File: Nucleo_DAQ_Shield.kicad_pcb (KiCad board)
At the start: 2 copper layers, 31 parts, among them J1 CONN_01X06, J2 CONN_01X06, J3 CONN_01X02, J4 CONN_01X02, J5 CONN_01X02, J6 CONN_COAXIAL, U1 4050, U10 ST_Nucleo144_F746ZG_CN10, U2 TL072, U3 LM7805CT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

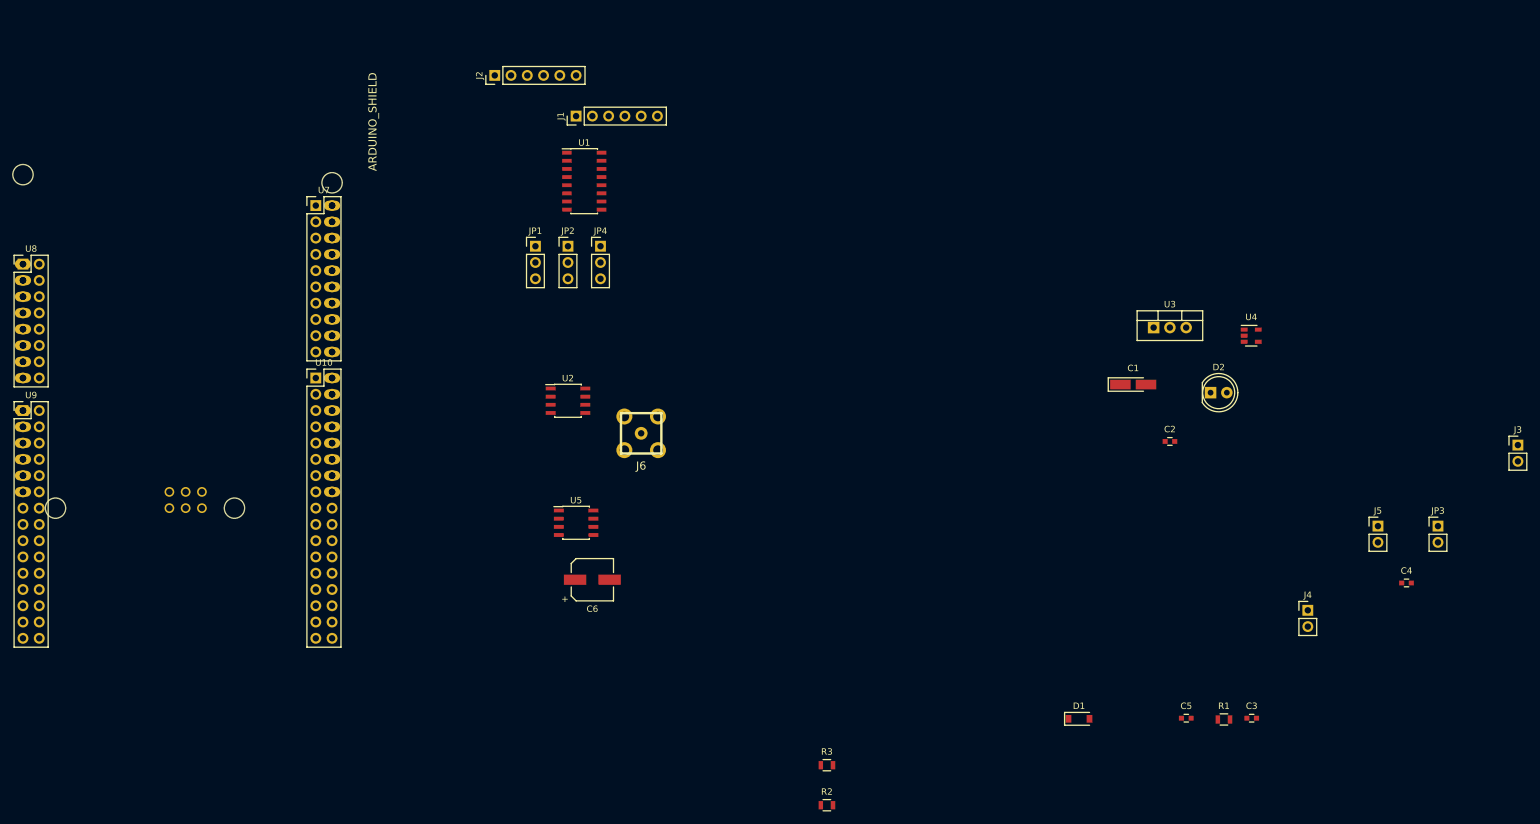
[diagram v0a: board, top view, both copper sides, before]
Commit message: Rough placement of all components
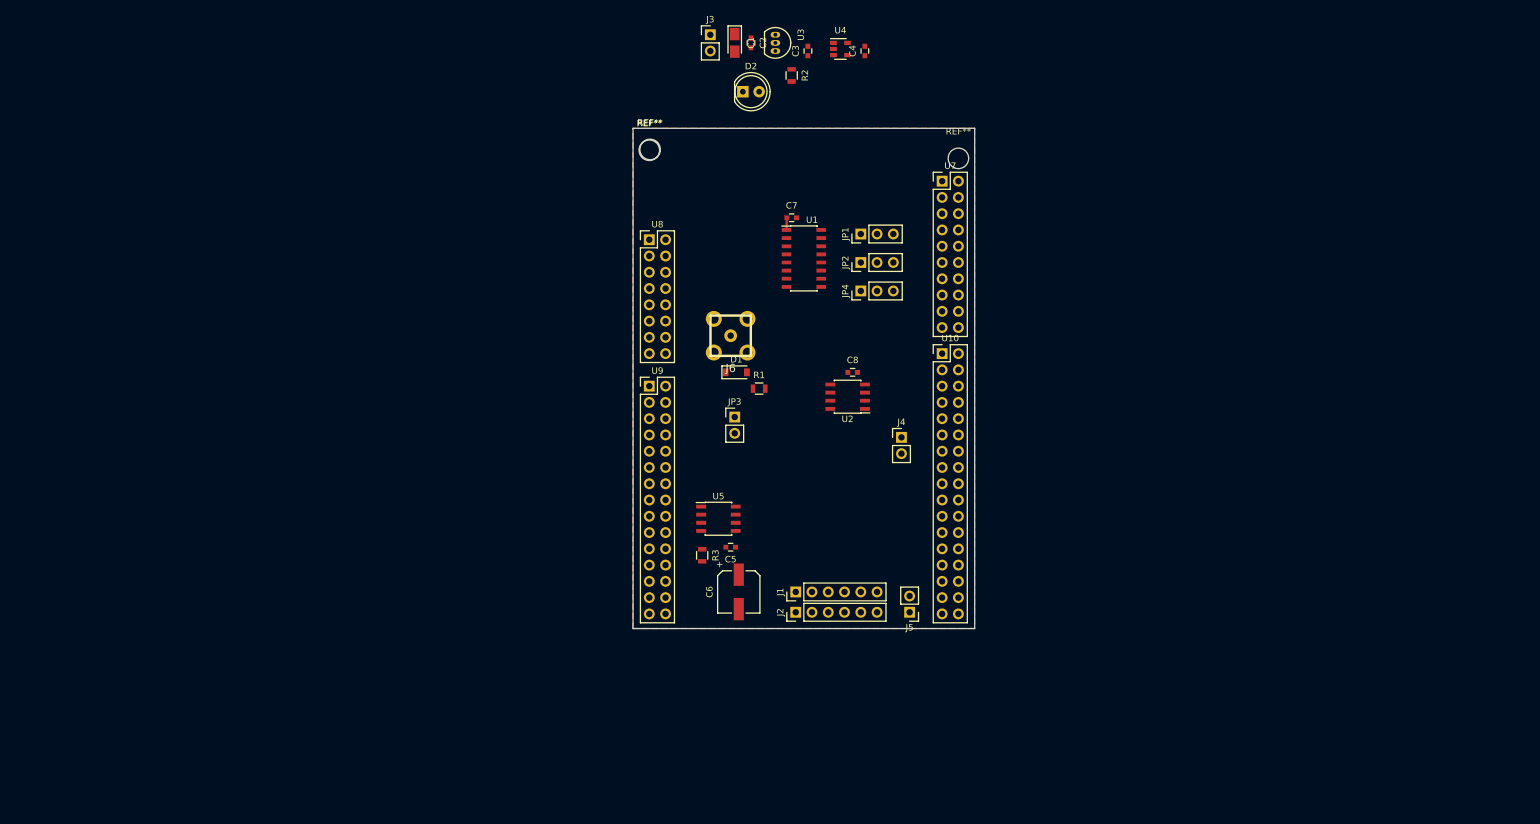
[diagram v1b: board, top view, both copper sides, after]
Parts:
- removed ARDUINO_SHIELD: val**, custom:ARDUINO_SHIELD
- added C7: 100nF, Capacitors_SMD:C_0603, F.Cu at (165.7, 62.9)
- added C8: 100nF, Capacitors_SMD:C_0603, F.Cu at (175.3, 87.0)
- added REF**: MountingHole_3.2mm_M3, Mounting_Holes:MountingHole_3.2mm_M3, F.Cu at (143.6, 52.2)
- added REF**: MountingHole_3.2mm_M3, Mounting_Holes:MountingHole_3.2mm_M3, F.Cu at (143.5, 52.3)
- added REF**: MountingHole_3.2mm_M3, Mounting_Holes:MountingHole_3.2mm_M3, F.Cu at (191.8, 53.6)
- C1: footprint Capacitors_Tantalum_SMD:CP_Tantalum_Case-A_EIA-3216-18_Hand -> Capacitors_Tantalum_SMD:CP_Tantalum_Case-A_EIA-3216-18_Reflow
- U3: footprint TO_SOT_Packages_THT:TO-220_Vertical -> TO_SOT_Packages_THT:TO-92_Inline_Narrow_Oval
- moved J3 141.4 mm to (153.0, 34.3)
- moved C3 125.1 mm to (168.3, 36.8), turned to 90 degrees
- moved C4 118.5 mm to (177.2, 36.8), turned to 90 degrees
- moved R2 114.1 mm to (165.7, 40.6), turned to 270 degrees
- moved JP3 111.1 mm to (156.8, 94.0)
- moved U10 97.9 mm to (189.2, 84.1)
- moved U7 97.9 mm to (189.2, 57.1)
- moved U8 97.9 mm to (143.5, 66.3)
- moved U9 97.9 mm to (143.5, 89.2)
- moved J2 96.1 mm to (166.4, 124.5)
- moved C2 90.3 mm to (159.4, 35.6), turned to 270 degrees
- moved R1 89.1 mm to (160.7, 89.5)
- moved D2 86.8 mm to (158.1, 43.2)
- moved C1 82.0 mm to (156.8, 35.6), turned to 270 degrees
- moved J1 81.8 mm to (166.4, 121.3)
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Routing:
- net +3.3VA: track 0.00 -> 2.40 mm
- added copper zone on F.Cu, net GND
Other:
- board outline added: 53.3 x 78.1 mm
- net class Default: clearance 0.2 -> 0.381; trace_width 0.25 -> 0.381
- rule trace_clearance: 0.2 -> 0.381

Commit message: --amend
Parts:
- added J7: CONN_01X02, Pin_Headers:Pin_Header_Straight_1x02_Pitch2.54mm, F.Cu at (174.0, 105.4)
- moved C7 43.0 mm to (177.8, 104.1)
- moved U1 43.0 mm to (179.7, 110.5)
- moved JP1 42.8 mm to (165.1, 106.7)
- moved JP2 41.0 mm to (165.1, 109.2)
- moved JP4 39.2 mm to (165.1, 111.8)
- moved C1 17.8 mm to (158.1, 53.3)
- moved C2 17.8 mm to (160.7, 53.3)
- moved C3 17.8 mm to (169.5, 54.6)
- moved C4 17.8 mm to (178.4, 54.6)
- moved D2 17.8 mm to (159.4, 61.0)
- moved J3 17.8 mm to (154.3, 52.1), turned to 270 degrees
- moved R2 17.8 mm to (167.0, 58.4)
- moved U3 17.8 mm to (164.5, 52.1)
- moved U4 17.8 mm to (174.6, 54.3)
- moved J4 14.9 mm to (177.8, 83.2)
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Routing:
- net +3.3VA: track 2.40 -> 0.00 mm

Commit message: Some progress on routing
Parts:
- moved R3 1.42 mm to (150.5, 114.9)
- moved JP1 1.27 mm to (165.1, 105.4)
- moved JP4 1.27 mm to (165.1, 113.0)
- moved C4 0.63 mm to (179.1, 54.6), turned to 270 degrees
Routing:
- net +5V: track 0.00 -> 103.6 mm, vias 0 -> 3
- net Vbat: track 0.00 -> 88.9 mm, vias 0 -> 3
- net /MOTOR-: track 0.00 -> 54.6 mm, vias 0 -> 1
- net GND: track 0.00 -> 46.9 mm, vias 0 -> 31
- net /MOTOR+: track 0.00 -> 23.9 mm, vias 0 -> 1
- net Net-(J6-Pad1): track 0.00 -> 8.09 mm, vias 0 -> 1
- net /MOTOR_PWM_FORWARD: track 0.00 -> 6.19 mm
- net Net-(D2-Pad2): track 0.00 -> 5.74 mm, vias 0 -> 1
- net /MOTOR_PWM_REVERSE: track 0.00 -> 5.66 mm
- net +3.3VA: track 0.00 -> 5.48 mm
- net Net-(R3-Pad1): track 0.00 -> 2.68 mm
- added copper zone on B.Cu, net +3.3VA
- added copper zone on B.Cu, net GND
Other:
- net class Power added: clearance 0.381, trace_width 0.762, via_dia 1.27, via_drill 0.762

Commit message: Mostly isolated AGND and DGND planes and fully routed analog portion; partially routed digital side
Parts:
- moved J7 6.38 mm to (173.4, 99.1)
- moved JP3 1.42 mm to (154.9, 80.6), turned to 0 degrees
- moved J1 1.27 mm to (166.4, 120.0)
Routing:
- net GND: track 46.9 -> 94.8 mm, vias 31 -> 35
- net /ENVLP_buffered: track 0.00 -> 30.5 mm, vias 0 -> 1
- net /GAIN: track 0.00 -> 16.7 mm
- net +3.3VA: track 5.48 -> 18.7 mm, vias 0 -> 3
- net Net-(J1-Pad4): track 0.00 -> 11.6 mm, vias 0 -> 1
- net /Tx_Pulse_buffered: track 0.00 -> 11.5 mm, vias 0 -> 1
- net /ENVLP: track 0.00 -> 10.4 mm
- net Net-(J1-Pad3): track 0.00 -> 9.31 mm, vias 0 -> 1
- net /GAIN_buffered: track 0.00 -> 6.24 mm, vias 0 -> 1
- net Net-(D1-Pad1): track 0.00 -> 4.97 mm, vias 0 -> 1
- net +5V: track 103.6 -> 103.0 mm
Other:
- board text added: "Area below is AGND (mostly isolated from DGND)"

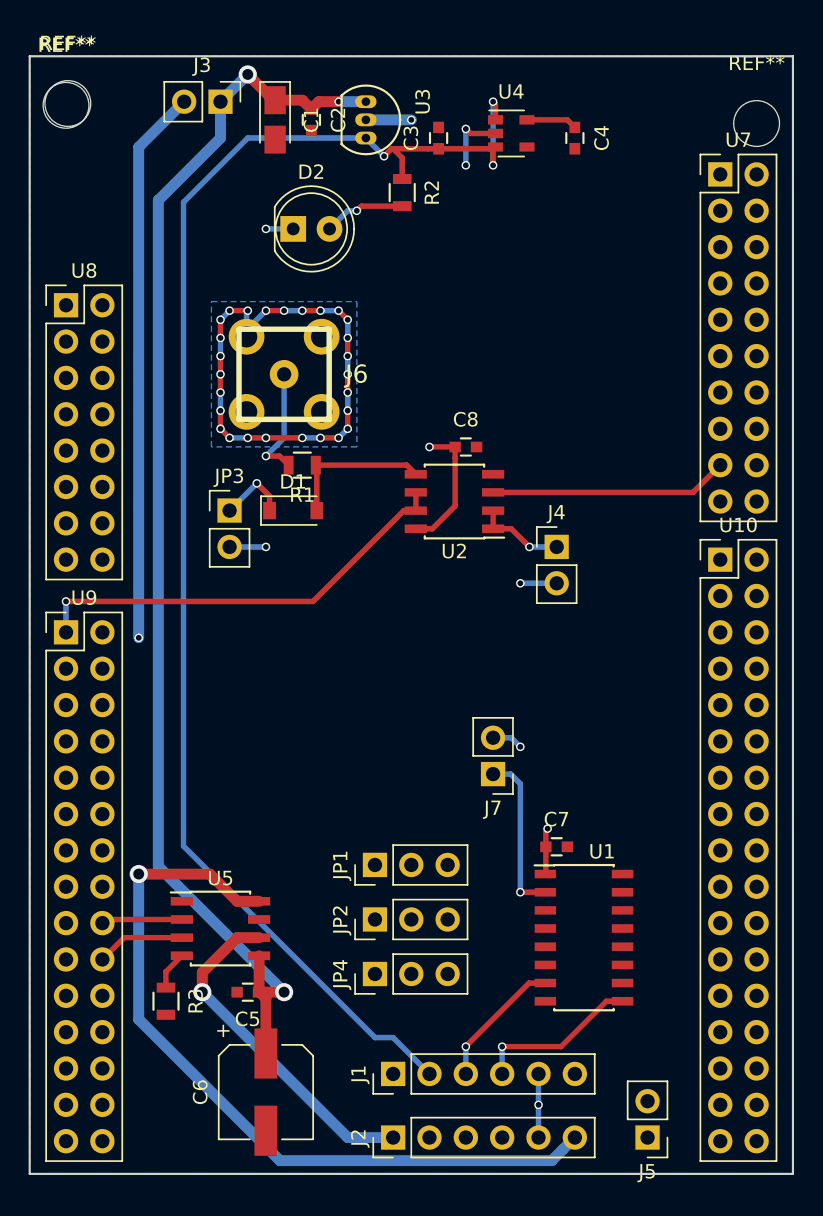
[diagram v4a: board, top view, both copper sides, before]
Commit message: Removed extraneous parts and finished PCB layout
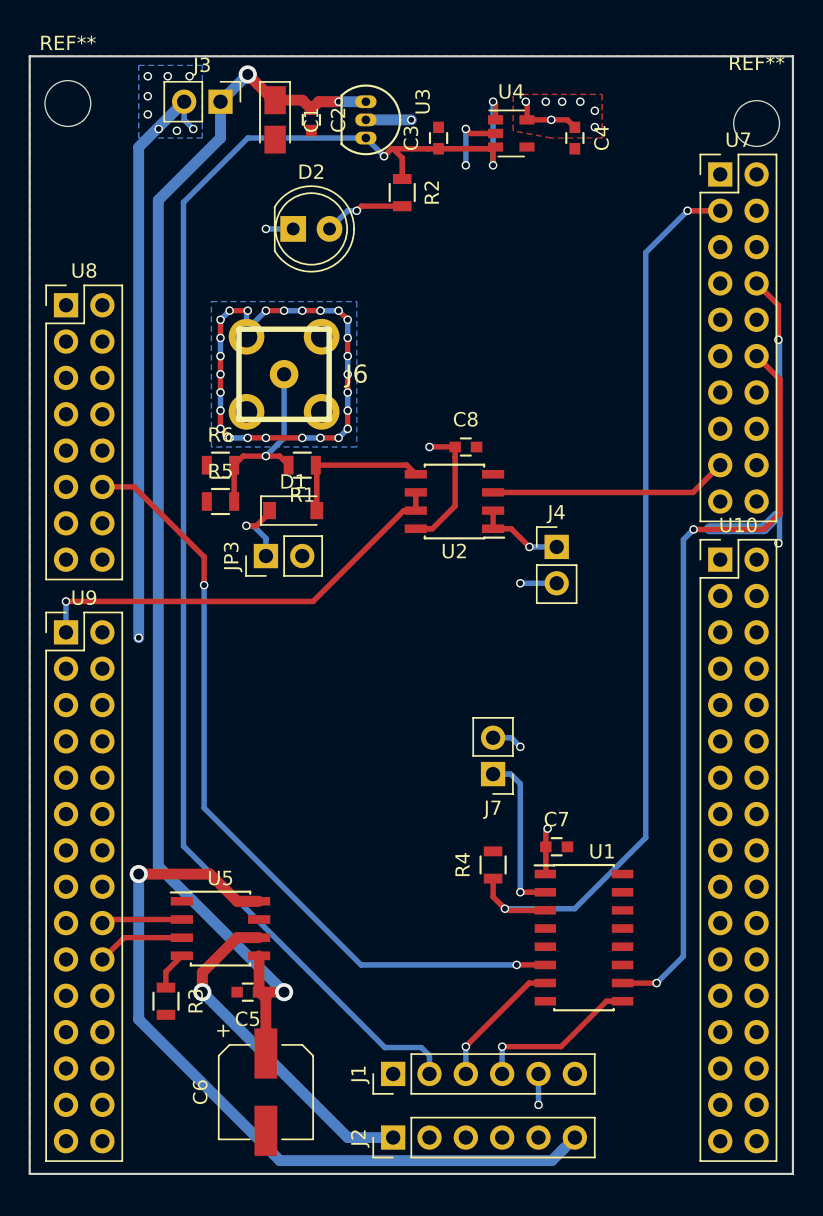
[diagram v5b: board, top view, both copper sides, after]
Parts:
- removed J5: CONN_01X02, Pin_Headers:Pin_Header_Straight_1x02_Pitch2.54mm
- removed JP1, JP2, JP4: Jumper_NC_Dual, Pin_Headers:Pin_Header_Straight_1x03_Pitch2.54mm
- removed the REF** at (143.5, 52.3)
- added R4: 100, Resistors_SMD:R_0805, F.Cu at (173.4, 105.4)
- added R5: 100, Resistors_SMD:R_0805, F.Cu at (154.3, 80.0)
- added R6: 100, Resistors_SMD:R_0805, F.Cu at (154.3, 77.5)
- moved JP3 4.07 mm to (157.5, 83.8), turned to 90 degrees
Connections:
- net Net-(J1-Pad3) renamed /5V_CUI_A
- net Net-(J1-Pad4) renamed /5V_CUI_X
- J2 pad 2: +3.3VA -> Net-(J2-Pad2)
- J2 pad 3: /Motor_encoder_A -> Net-(J2-Pad3)
- J2 pad 4: /Motor_encoder_B -> Net-(J2-Pad4)
- J2 pad 5: GND -> Net-(J2-Pad5)
- U1 pad 1: +3.3VA -> VCC
- U1 pad 10: /CUI_encoder_X -> /ENCODER_X
- U1 pad 11: Net-(J5-Pad1) -> (no net)
- U1 pad 12: /Ext_index -> (no net)
- U1 pad 4: /CUI_encoder_B -> (no net)
- U1 pad 5: Net-(J1-Pad1) -> (no net)
- U1 pad 6: /CUI_encoder_A -> /ENCODER_A
- U1 pad 8: GND -> VSS
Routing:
- net /Tx_Pulse: track 0.00 -> 64.5 mm, vias 0 -> 2
- net /ENCODER_A: track 0.00 -> 55.1 mm, vias 0 -> 2
- net /ENCODER_X: track 0.00 -> 53.3 mm, vias 0 -> 2
- net GND: track 94.8 -> 118.8 mm, vias 35 -> 45
- net Net-(J6-Pad1): track 8.09 -> 13.1 mm
- net +3.3VA: track 18.7 -> 15.5 mm, vias 3 -> 9
- net VCC: track 0.00 -> 1.92 mm
- net +5V: track 103.0 -> 103.8 mm
- added copper zone on F.Cu, net +3.3VA
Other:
- board text added: "AGND"
- board text added: "DGND"
- board text added: "Pins for the Nucleo headers will be mounted upside down, so tracks should connect to them on F.Cu All other header pins will be mounted normally, so tracks should connect to them on B.Cu"

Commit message: Finalized v1.0 of PCB design
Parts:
- added REF***: OSHW-Logo_7.5x8mm_SilkScreen, Symbols:OSHW-Logo_7.5x8mm_SilkScreen, F.Cu at (175.9, 68.3)
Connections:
- U1 pad 1: VCC -> +3.3VA
- U1 pad 8: VSS -> GND
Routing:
- net GND: track 118.8 -> 134.1 mm, vias 45 -> 44
- net +3.3VA: track 15.5 -> 23.7 mm
- net VCC: track 1.92 -> 0.00 mm
- net /ENVLP_buffered: track 30.5 -> 30.0 mm, vias 1 -> 0
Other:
- net class Default: clearance 0.381 -> 0.254
- rule trace_clearance: 0.381 -> 0.254
- board text added: "AGND zone"
- board text added: "DGND track"
- board text added: "DGND zone"
- board text added: "Nucleo DAQ Shield Columbia University Creative Machines Lab"
- board text removed: "Area below is AGND (mostly isolated from DGND)"
